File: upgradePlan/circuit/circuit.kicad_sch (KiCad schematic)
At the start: 34 parts, among them J1 Connector_GY_521, J2 Conn_VL53L0/1xV2, J3 Conn_HC_SR04, M1 Motor_DC, M2 Motor_Servo, Q1 BD249, Q2 BD249, Q4 BD249, SW1 SW_DIP_x01, U1 Freenove-SP32-WROVER, U2 L293D, U3 LM350_TO220, U4 LM350_TO220, U5 LM317_TO-220

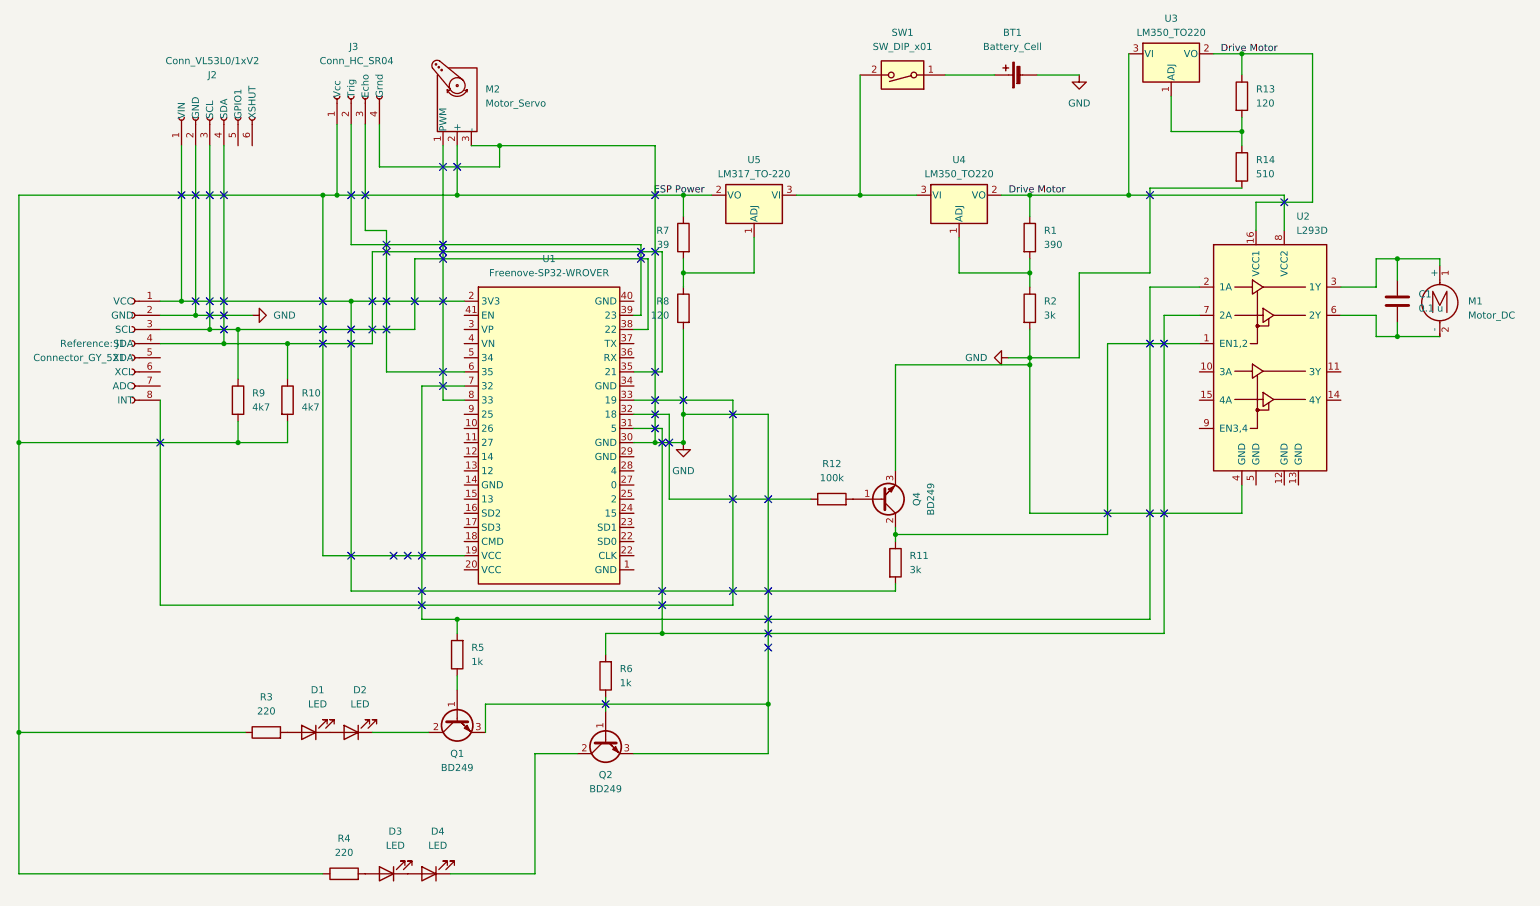
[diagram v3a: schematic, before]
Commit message: added footprints to schematic and board edge
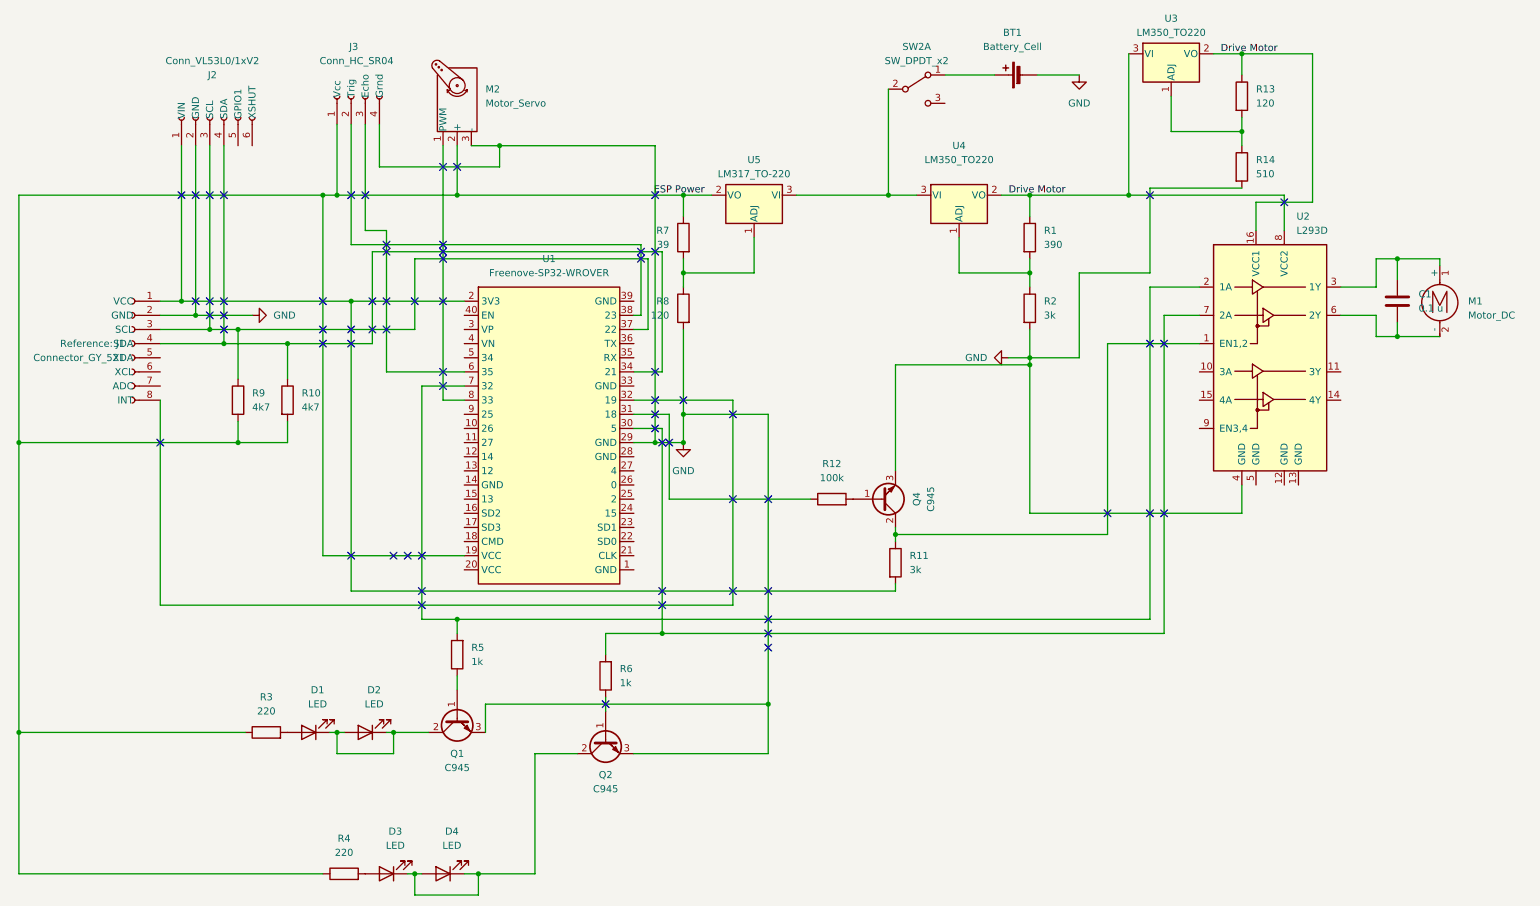
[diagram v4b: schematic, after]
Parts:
- removed SW1: SW_DIP_x01, symbol Switch:SW_DIP_x01
- added SW2: SW_DPDT_x2, Button_Switch_THT:SW_Slide_1P2T_CK_OS102011MS2Q, symbol Switch:SW_DPDT_x2
- BT1: footprint (none) -> Connector_AMASS:AMASS_XT60-M_1x02_P7.20mm_Vertical
- D1, D3, M1: footprint (none) -> Connector_Phoenix_SPT:PhoenixContact_SPT_2.5_2-V-5.0-EX_1x02_P5.0mm_Vertical
- J1: footprint (none) -> Connector_PinSocket_2.54mm:PinSocket_1x08_P2.54mm_Vertical
- J2: footprint (none) -> Connector_PinHeader_2.54mm:PinHeader_1x06_P2.54mm_Horizontal
- J3: footprint (none) -> Connector_PinHeader_2.54mm:PinHeader_1x04_P2.54mm_Horizontal
- M2: footprint (none) -> Connector_PinHeader_2.54mm:PinHeader_1x03_P2.54mm_Horizontal
- Q1, Q2, Q4: value BD249 -> C945; footprint (none) -> Package_TO_SOT_THT:TO-92
- R1, R10, R11, R12, R13, R14, R2, R3, R4, R5, R6, R7, R8, R9: footprint (none) -> Resistor_THT:R_Axial_DIN0207_L6.3mm_D2.5mm_P15.24mm_Horizontal
- U1: footprint RF_Module:Freenove-ESP32-WROVER -> MyESPConnector:MyESPConnector
- U3, U4, U5: footprint Package_TO_SOT_THT:TO-220-3_Vertical -> Package_TO_SOT_THT:TO-220-3_Horizontal_TabDown
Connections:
- net GND: now also U1.29 (GND); no longer U1.30 (GND)
- net at D3.1 (K), D4.2 (A): now also D4.1 (K), Q2.2 (C)
- net at BT1.1 (+): now also SW2.1 (A)
- net at U4.3 (VI), U5.3 (VI): now also SW2.2 (B)
- net at J1.4 (SDA), J2.4 (SDA), R10.1: now also U1.34 (21); no longer U1.35 (21)
- net at D2.1 (K), Q1.2 (C): now also D1.1 (K), D2.2 (A)
- net at R6.2, U2.7 (2A): now also U1.30 (5); no longer U1.31 (5)
- net at J1.3 (SCL), J2.3 (SCL), R9.1: now also U1.37 (22); no longer U1.38 (22)
- net at J1.8 (INT): now also U1.32 (19); no longer U1.33 (19)
- net at J3.2 (Trig): now also U1.38 (23); no longer U1.39 (23)
- net at R12.1: now also U1.31 (18); no longer U1.32 (18)
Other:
- moved on the sheet: D2, D4

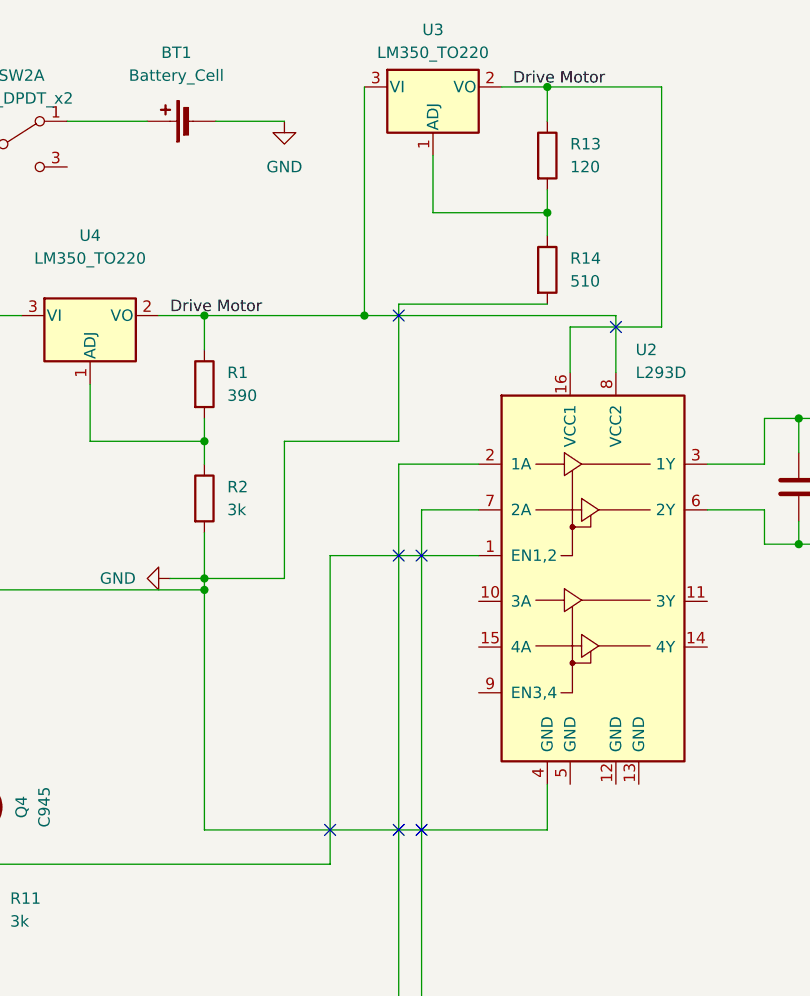
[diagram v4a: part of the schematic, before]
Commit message: added front routing with auto completed back
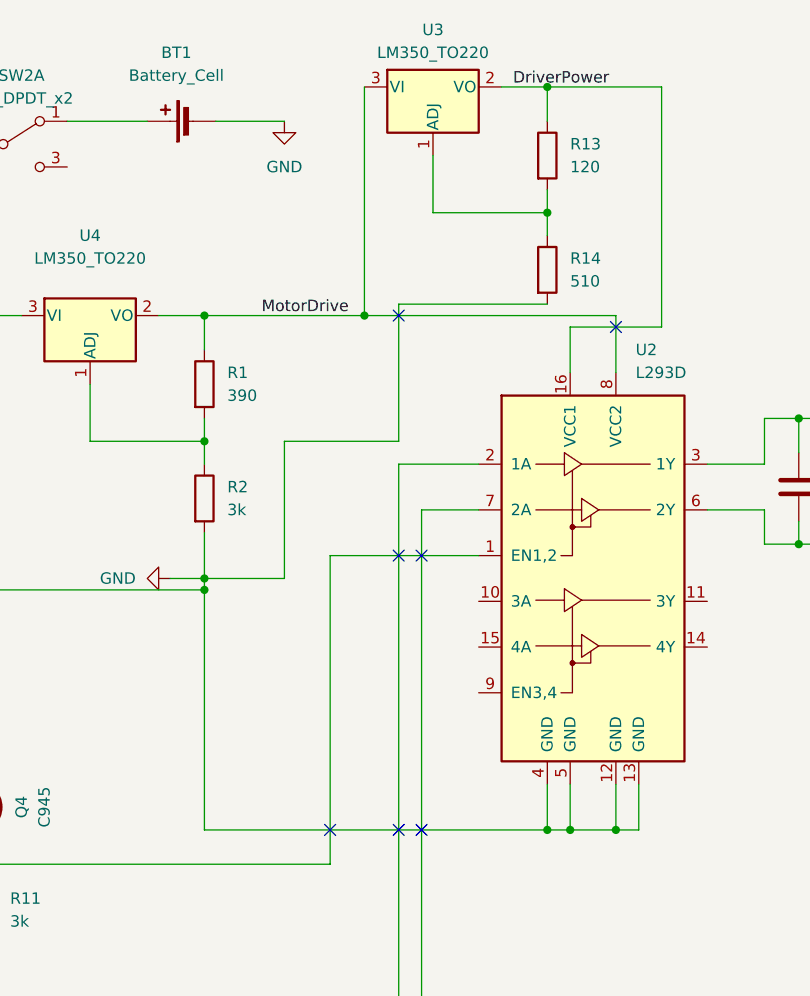
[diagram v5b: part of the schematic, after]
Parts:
- J1: footprint Connector_PinSocket_2.54mm:PinSocket_1x08_P2.54mm_Vertical -> MyESPConnector:GY-521
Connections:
- net GND: now also U2.12 (GND), U2.13 (GND), U2.5 (GND)
- net Drive Motor renamed MotorDrive
- net MotorDrive: no longer R13.1, U2.16 (VCC1), U3.2 (VO)
- new net DriverPower: R13.1, U2.16 (VCC1), U3.2 (VO)
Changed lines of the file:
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@@
   (junction (at 176.53 107.95) (diameter 0) (color 0 0 0 0)
   )
+  (junction (at 241.3 104.14) (diameter 0) (color 0 0 0 0)
+  )
   (junction (at 76.2 46.99) (diameter 0) (color 0 0 0 0)
   )
@@
   (junction (at 138.43 60.96) (diameter 0) (color 0 0 0 0)
   )
+  (junction (at 238.76 104.14) (diameter 0) (color 0 0 0 0)
+  )
   (junction (at 78.74 66.04) (diameter 0) (color 0 0 0 0)
   )
@@
   )
   (junction (at 19.05 143.51) (diameter 0) (color 0 0 0 0)
+  )
+  (junction (at 246.38 104.14) (diameter 0) (color 0 0 0 0)
   )
   (junction (at 76.2 143.51) (diameter 0) (color 0 0 0 0)
@@
   (no_connect (at 130.81 57.15))
   (no_connect (at 97.79 41.91))
+  (no_connect (at 246.38 48.26))
   (no_connect (at 85.09 71.12))
   (no_connect (at 133.35 57.15))
@@
   (no_connect (at 55.88 46.99))
   (no_connect (at 214.63 104.14))
-  (no_connect (at 246.38 48.26))
   (no_connect (at 55.88 71.12))
   (no_connect (at 91.44 118.11))
@@
     (stroke (width 0) (type default))
   )
+  (wire (pts (xy 241.3 104.14) (xy 246.38 104.14))
+    (stroke (width 0) (type default))
+  )
   (wire (pts (xy 241.3 48.26) (xy 241.3 53.34))
     (stroke (width 0) (type default))
@@
     (stroke (width 0) (type default))
   )
+  (wire (pts (xy 238.76 104.14) (xy 241.3 104.14))
+    (stroke (width 0) (type default))
+  )
   (wire (pts (xy 151.13 54.61) (xy 151.13 60.96))
     (stroke (width 0) (type default))
@@
     (stroke (width 0) (type default))
   )
+  (wire (pts (xy 246.38 99.06) (xy 246.38 104.14))
+    (stroke (width 0) (type default))
+  )
   (wire (pts (xy 134.62 125.73) (xy 224.79 125.73))
     (stroke (width 0) (type default))
@@
     (stroke (width 0) (type default))
   )
+  (wire (pts (xy 241.3 99.06) (xy 241.3 104.14))
+    (stroke (width 0) (type default))
+  )
   (wire (pts (xy 97.79 123.19) (xy 222.25 123.19))
     (stroke (width 0) (type default))
@@
     (stroke (width 0) (type default))
   )
+  (wire (pts (xy 248.92 104.14) (xy 248.92 99.06))
+    (stroke (width 0) (type default))
+  )
   (wire (pts (xy 135.89 86.36) (xy 135.89 101.6))
     (stroke (width 0) (type default))
@@
   )
   (wire (pts (xy 76.2 147.32) (xy 86.36 147.32))
+    (stroke (width 0) (type default))
+  )
+  (wire (pts (xy 246.38 104.14) (xy 248.92 104.14))
     (stroke (width 0) (type default))
   )
@@
     (effects (font (size 1.27 1.27)) (justify right bottom))
   )
-  (label "Drive Motor" (at 234.95 21.59 0) (fields_autoplaced)
+  (label "DriverPower" (at 234.95 21.59 0) (fields_autoplaced)
     (effects (font (size 1.27 1.27)) (justify left bottom))
   )
-  (label "Drive Motor" (at 196.85 46.99 0) (fields_autoplaced)
+  (label "MotorDrive" (at 207.01 46.99 0) (fields_autoplaced)
     (effects (font (size 1.27 1.27)) (justify left bottom))
   )
@@
       (effects (font (size 1.27 1.27)) (justify left))
     )
-    (property "Footprint" "Connector_PinSocket_2.54mm:PinSocket_1x08_P2.54mm_Vertical" (at 39.37 73.66 0)
-      (effects (font (size 1.27 1.27)) hide)
-    )
+    (property "Footprint" "MyESPConnector:GY-521" (at 39.37 73.66 0)
+      (effects (font (size 1.27 1.27)) hide)
+    )

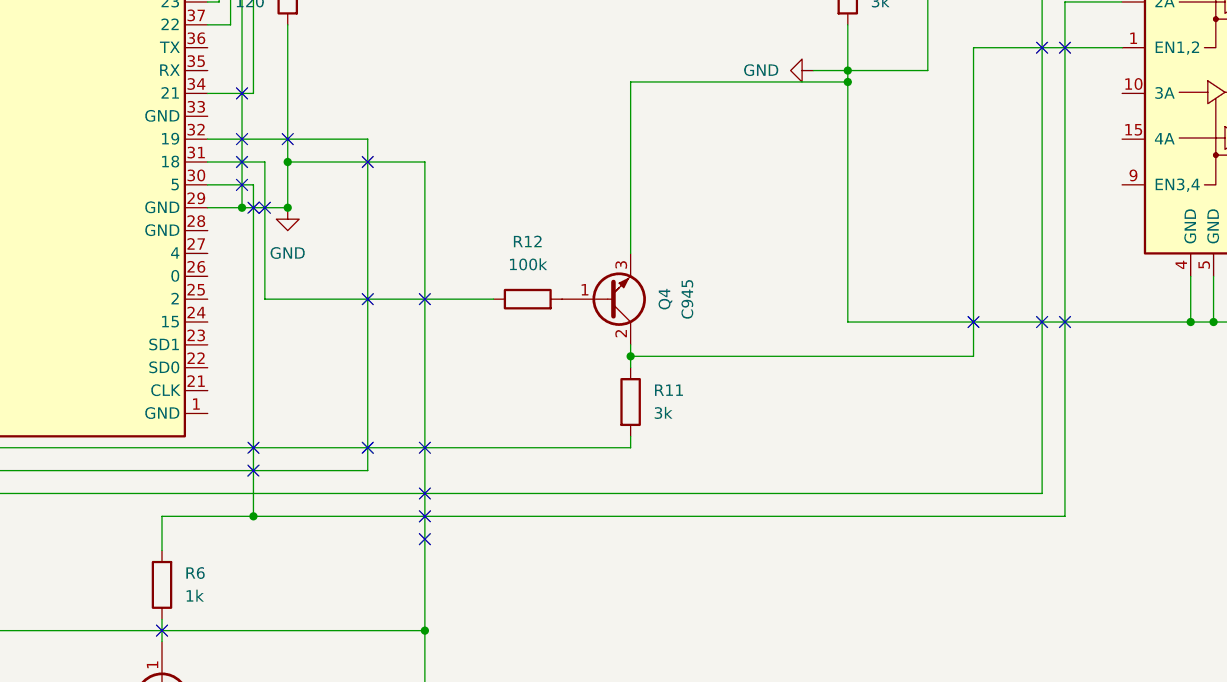
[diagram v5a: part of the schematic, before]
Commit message: FIxed wrong copnnection in pcb and updated code correspondingly. Switch pin 31 and 30.
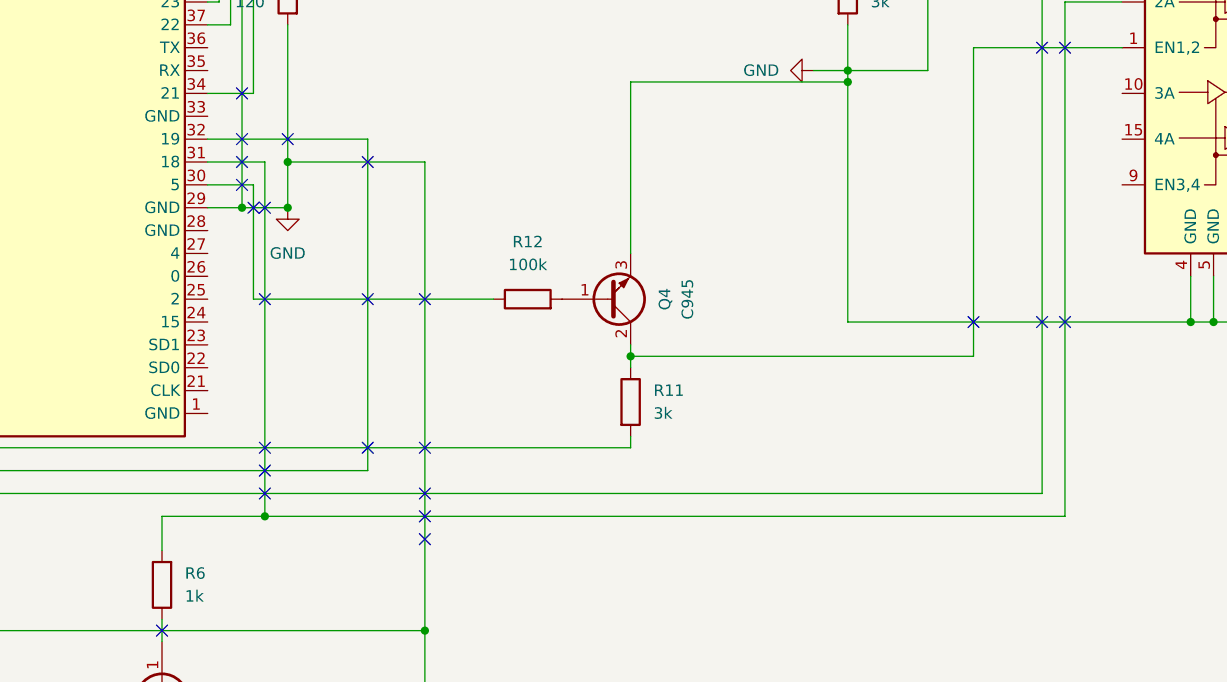
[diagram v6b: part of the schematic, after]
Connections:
- net at R6.2, U2.7 (2A): now also U1.31 (18); no longer U1.30 (5)
- net at R12.1: now also U1.30 (5); no longer U1.31 (18)
- no-connect marks 68 -> 70
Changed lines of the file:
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@@
   (junction (at 175.26 46.99) (diameter 0) (color 0 0 0 0)
   )
-  (junction (at 134.62 125.73) (diameter 0) (color 0 0 0 0)
-  )
   (junction (at 138.43 60.96) (diameter 0) (color 0 0 0 0)
   )
@@
   )
   (junction (at 53.34 71.12) (diameter 0) (color 0 0 0 0)
+  )
+  (junction (at 135.89 125.73) (diameter 0) (color 0 0 0 0)
   )
   (junction (at 86.36 143.51) (diameter 0) (color 0 0 0 0)
@@
   (no_connect (at 50.8 46.99))
   (no_connect (at 85.09 66.04))
+  (no_connect (at 135.89 101.6))
   (no_connect (at 95.25 81.28))
   (no_connect (at 95.25 55.88))
@@
   (no_connect (at 95.25 58.42))
   (no_connect (at 73.66 73.66))
+  (no_connect (at 135.89 118.11))
   (no_connect (at 147.32 101.6))
   (no_connect (at 153.67 128.27))
-  (no_connect (at 134.62 120.65))
   (no_connect (at 95.25 41.91))
+  (no_connect (at 135.89 123.19))
   (no_connect (at 135.89 91.44))
   (no_connect (at 222.25 73.66))
   (no_connect (at 222.25 104.14))
   (no_connect (at 50.8 66.04))
-  (no_connect (at 134.62 118.11))
   (no_connect (at 133.35 78.74))
   (no_connect (at 73.66 66.04))
@@
   (no_connect (at 97.79 41.91))
   (no_connect (at 246.38 48.26))
+  (no_connect (at 135.89 120.65))
   (no_connect (at 85.09 71.12))
   (no_connect (at 133.35 57.15))
@@
     (stroke (width 0) (type default))
   )
+  (wire (pts (xy 134.62 88.9) (xy 134.62 101.6))
+    (stroke (width 0) (type default))
+  )
   (wire (pts (xy 266.7 58.42) (xy 266.7 62.23))
     (stroke (width 0) (type default))
@@
     (stroke (width 0) (type default))
   )
+  (wire (pts (xy 135.89 125.73) (xy 224.79 125.73))
+    (stroke (width 0) (type default))
+  )
   (wire (pts (xy 138.43 60.96) (xy 138.43 63.5))
     (stroke (width 0) (type default))
@@
     (stroke (width 0) (type default))
   )
-  (wire (pts (xy 135.89 101.6) (xy 161.29 101.6))
-    (stroke (width 0) (type default))
-  )
   (wire (pts (xy 251.46 48.26) (xy 241.3 48.26))
     (stroke (width 0) (type default))
@@
     (stroke (width 0) (type default))
   )
+  (wire (pts (xy 135.89 86.36) (xy 135.89 125.73))
+    (stroke (width 0) (type default))
+  )
   (wire (pts (xy 151.13 60.96) (xy 138.43 60.96))
     (stroke (width 0) (type default))
@@
     (stroke (width 0) (type default))
   )
-  (wire (pts (xy 124.46 125.73) (xy 134.62 125.73))
+  (wire (pts (xy 124.46 125.73) (xy 135.89 125.73))
     (stroke (width 0) (type default))
   )
@@
     (stroke (width 0) (type default))
   )
-  (wire (pts (xy 134.62 125.73) (xy 224.79 125.73))
-    (stroke (width 0) (type default))
-  )
   (wire (pts (xy 76.2 34.29) (xy 76.2 46.99))
     (stroke (width 0) (type default))
@@
     (stroke (width 0) (type default))
   )
-  (wire (pts (xy 135.89 86.36) (xy 135.89 101.6))
-    (stroke (width 0) (type default))
-  )
   (wire (pts (xy 99.06 81.28) (xy 91.44 81.28))
     (stroke (width 0) (type default))
@@
     (stroke (width 0) (type default))
   )
-  (wire (pts (xy 134.62 125.73) (xy 134.62 88.9))
-    (stroke (width 0) (type default))
-  )
   (wire (pts (xy 134.62 78.74) (xy 134.62 57.15))
     (stroke (width 0) (type default))
@@
     (stroke (width 0) (type default))
   )
+  (wire (pts (xy 161.29 101.6) (xy 134.62 101.6))
+    (stroke (width 0) (type default))
+  )
